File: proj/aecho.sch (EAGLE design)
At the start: 47 parts, among them J3 SJ1-3523N, P1 I2C(SCL-SDA), P2 MP3_CTL(SCKR-SDI-DREQ-RST), P3 AMP_CTL(SHDN-CLK-UPDN), P4 PWR(GND-VIN-GND), P9 AOUT_L-GND-AOUT_R, U10 CS4334, U11 LM4811PDSO-10, U12 5.0V, U7 3.3V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

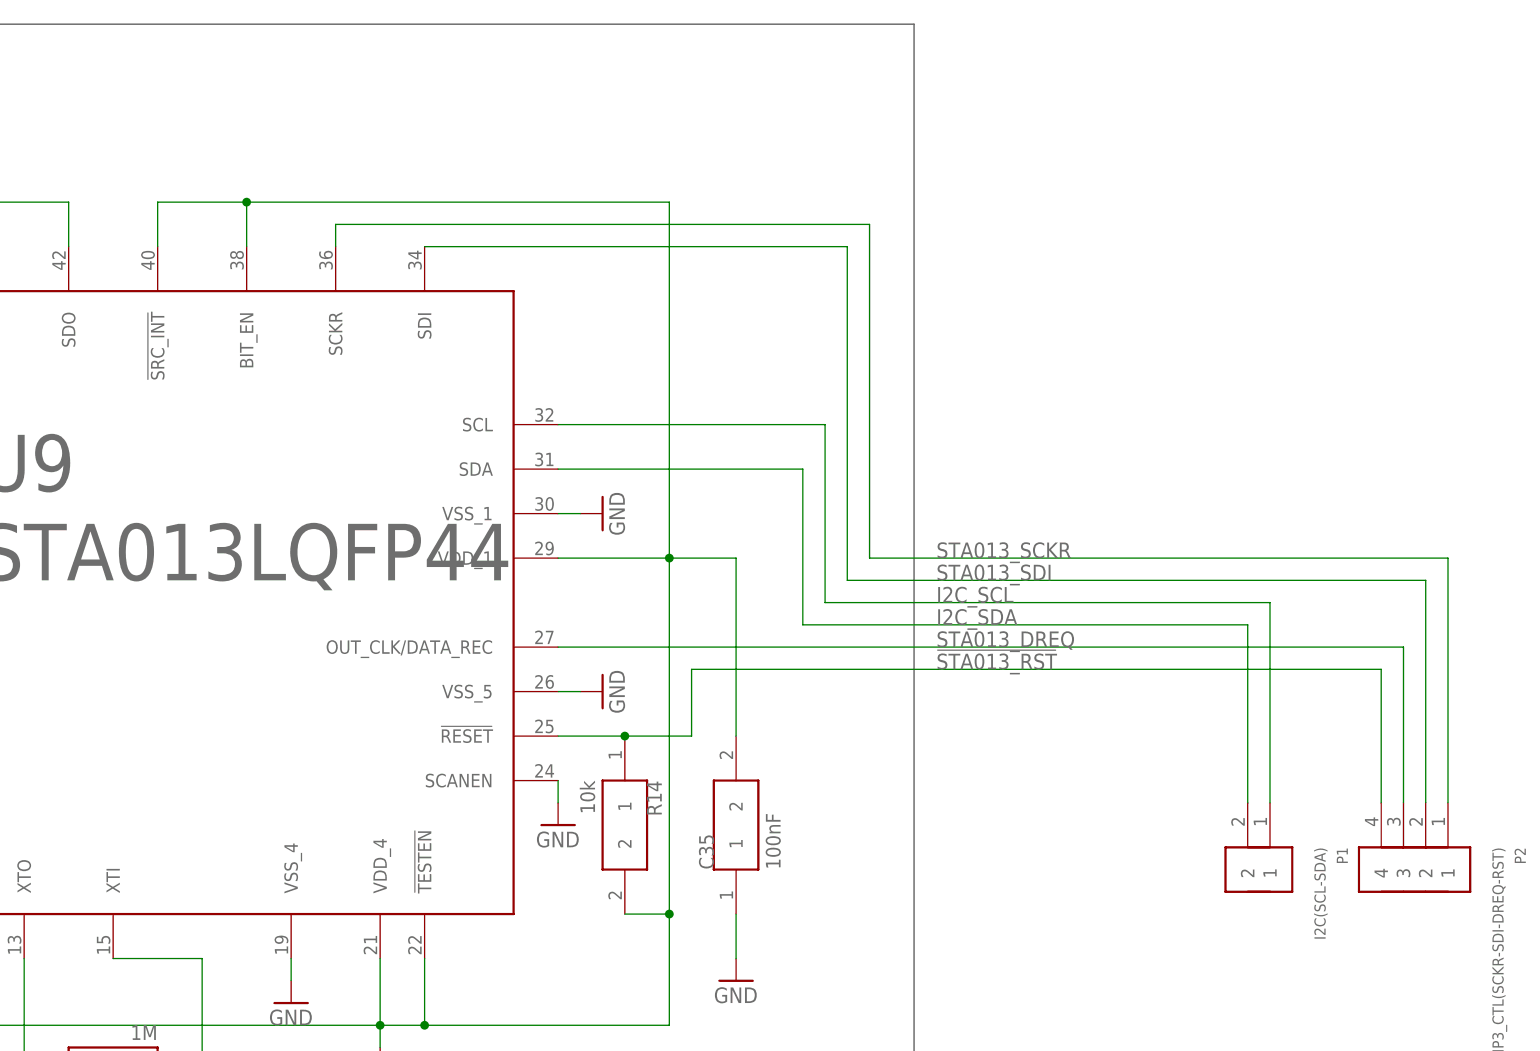
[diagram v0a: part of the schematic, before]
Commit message: @open #9 @open #4 @close #4 Exposed STA013 BIT_EN line in Aecho module
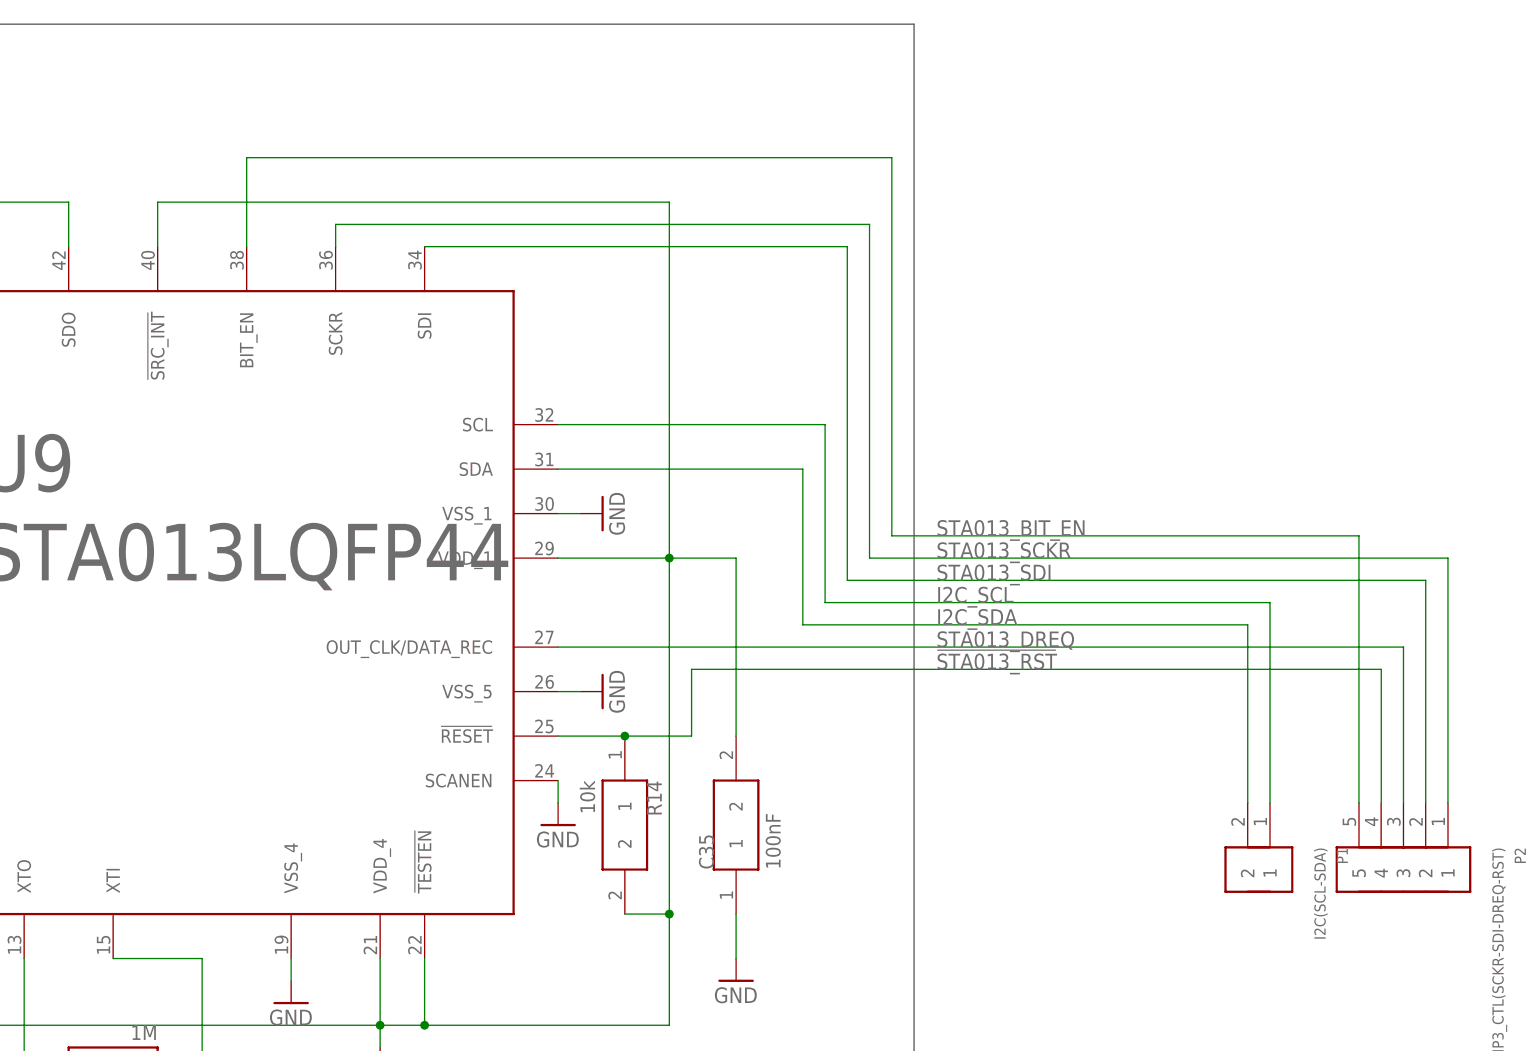
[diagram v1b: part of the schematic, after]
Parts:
- P2: device dooba:PIN_4 -> dooba:PIN_5
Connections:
- new net STA013_BIT_EN: P2.5, U9.BIT_EN
- net 3.3V: no longer U9.BIT_EN
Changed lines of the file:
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@@
 <layer number="115" name="ReferenceISLANDS" color="7" fill="1" visible="yes" active="yes"/>
 <layer number="116" name="Patch_BOT" color="9" fill="4" visible="yes" active="yes"/>
+<layer number="117" name="Refs" color="11" fill="1" visible="yes" active="yes"/>
 <layer number="118" name="Rect_Pads" color="7" fill="1" visible="yes" active="yes"/>
 <layer number="121" name="_tsilk" color="7" fill="1" visible="yes" active="yes"/>
@@
 <part name="GND110" library="supply1" deviceset="GND" device=""/>
 <part name="P1" library="dooba" deviceset="PIN_2" device="" value="I2C(SCL-SDA)"/>
-<part name="P2" library="dooba" deviceset="PIN_4" device="" value="MP3_CTL(SCKR-SDI-DREQ-RST)"/>
+<part name="P2" library="dooba" deviceset="PIN_5" device="" value="MP3_CTL(SCKR-SDI-DREQ-RST)"/>
 <part name="P3" library="dooba" deviceset="PIN_3" device="" value="AMP_CTL(SHDN-CLK-UPDN)"/>
 <part name="P4" library="dooba" deviceset="PIN_3" device="" value="PWR(GND-VIN-GND)"/>
@@
 <pinref part="U9" gate="U1" pin="!SRC_INT"/>
 <wire x1="210.82" y1="203.2" x2="210.82" y2="208.28" width="0.1524" layer="91"/>
-<wire x1="210.82" y1="208.28" x2="220.98" y2="208.28" width="0.1524" layer="91"/>
-<pinref part="U9" gate="U1" pin="BIT_EN"/>
-<wire x1="220.98" y1="208.28" x2="220.98" y2="203.2" width="0.1524" layer="91"/>
-<wire x1="220.98" y1="208.28" x2="269.24" y2="208.28" width="0.1524" layer="91"/>
-<junction x="220.98" y="208.28"/>
+<wire x1="210.82" y1="208.28" x2="269.24" y2="208.28" width="0.1524" layer="91"/>
 <pinref part="U9" gate="U1" pin="VDD_1"/>
 <wire x1="256.54" y1="167.64" x2="269.24" y2="167.64" width="0.1524" layer="91"/>
@@
 </segment>
 </net>
+<net name="STA013_BIT_EN" class="0">
+<segment>
+<pinref part="U9" gate="U1" pin="BIT_EN"/>
+<wire x1="220.98" y1="203.2" x2="220.98" y2="213.36" width="0.1524" layer="91"/>
+<wire x1="220.98" y1="213.36" x2="294.64" y2="213.36" width="0.1524" layer="91"/>
+<wire x1="294.64" y1="213.36" x2="294.64" y2="170.18" width="0.1524" layer="91"/>
+<wire x1="294.64" y1="170.18" x2="347.98" y2="170.18" width="0.1524" layer="91"/>
+<label x="299.72" y="170.18" size="1.778" layer="95"/>
+<pinref part="P2" gate="P1" pin="5"/>
+<wire x1="347.98" y1="139.7" x2="347.98" y2="170.18" width="0.1524" layer="91"/>
+</segment>
+</net>

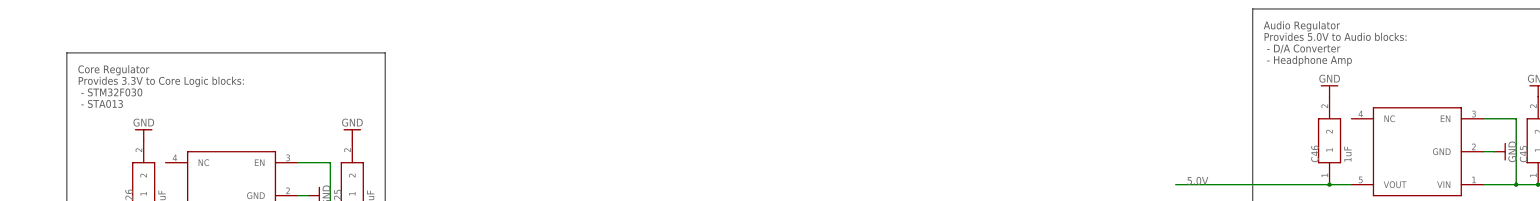
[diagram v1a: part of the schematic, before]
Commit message: Completed mobile phone (untitled) schematic Started routing mobile phone board
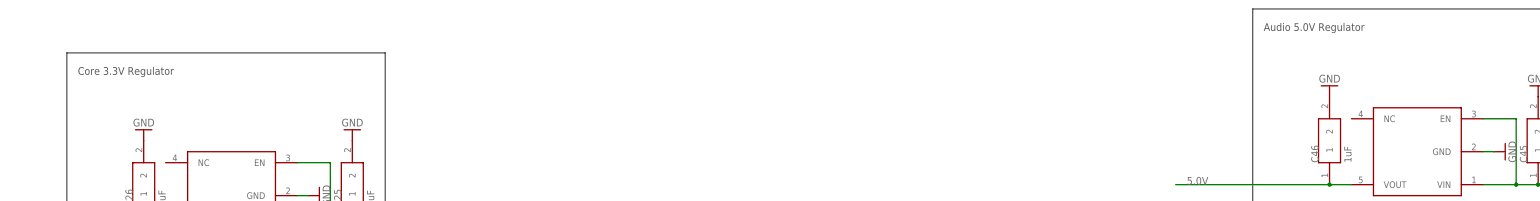
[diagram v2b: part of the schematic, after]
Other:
- note added: "Audio 5.0V Regulator"
- note added: "Core 3.3V Regulator"
- note removed: "Audio Regulator Provides 5.0V to Audio blocks: - D/A Converter - Headphone Amp"
- note removed: "Core Regulator Provides 3.3V to Core Logic blocks: - STM32F030 - STA013"
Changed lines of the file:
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@@
 <?xml version="1.0" encoding="utf-8"?>
 <!DOCTYPE eagle SYSTEM "eagle.dtd">
-<eagle version="7.3.0">
+<eagle version="8.4.0">
 <drawing>
 <settings>
 <setting alwaysvectorfont="no"/>
+<setting keepoldvectorfont="yes"/>
 <setting verticaltext="up"/>
 </settings>
@@
 <wire x1="195.58" y1="236.22" x2="121.92" y2="236.22" width="0.1524" layer="97"/>
 <wire x1="121.92" y1="236.22" x2="121.92" y2="292.1" width="0.1524" layer="97"/>
-<text x="124.46" y="279.4" size="1.778" layer="97">Core Regulator
-Provides 3.3V to Core Logic blocks:
- - STM32F030
- - STA013</text>
+<text x="124.46" y="287.02" size="1.778" layer="97">Core 3.3V Regulator</text>
 <wire x1="121.92" y1="228.6" x2="121.92" y2="58.42" width="0.1524" layer="97"/>
 <wire x1="121.92" y1="58.42" x2="297.18" y2="58.42" width="0.1524" layer="97"/>
@@
 <wire x1="469.9" y1="246.38" x2="396.24" y2="246.38" width="0.1524" layer="97"/>
 <wire x1="396.24" y1="246.38" x2="396.24" y2="302.26" width="0.1524" layer="97"/>
-<text x="398.78" y="289.56" size="1.778" layer="97">Audio Regulator
-Provides 5.0V to Audio blocks:
- - D/A Converter
- - Headphone Amp</text>
+<text x="398.78" y="297.18" size="1.778" layer="97">Audio 5.0V Regulator</text>
 <wire x1="396.24" y1="137.16" x2="551.18" y2="137.16" width="0.1524" layer="97"/>
 <wire x1="551.18" y1="137.16" x2="551.18" y2="58.42" width="0.1524" layer="97"/>
